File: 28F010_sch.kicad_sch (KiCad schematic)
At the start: 13 parts, among them U10 74LVC1G332, U11 74LS138, U12 CY7C199, U15 CY7C199, U16 4012, U17 CY7C199, U3 74LS04, U39 74LS04, U40 4012, U8 74LS138, U9 CY7C199

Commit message: pcb wiring
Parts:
- U16: footprint Package_DIP:DIP-12_W7.62mm -> (none)
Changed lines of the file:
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@@
     (property "Reference" "U16" (id 0) (at 111.76 8.89 0))
     (property "Value" "4012" (id 1) (at 111.76 11.43 0))
-    (property "Footprint" "Package_DIP:DIP-12_W7.62mm" (id 2) (at 111.76 19.05 0)
+    (property "Footprint" "" (id 2) (at 111.76 19.05 0)
       (effects (font (size 1.27 1.27)) hide)
     )
@@
     (property "Reference" "U16" (id 0) (at 111.76 19.05 0))
     (property "Value" "4012" (id 1) (at 111.76 21.59 0))
-    (property "Footprint" "Package_DIP:DIP-12_W7.62mm" (id 2) (at 111.76 29.21 0)
-      (effects (font (size 1.27 1.27)) hide)
-    )
+    (property "Footprint" "" (id 2) (at 111.76 29.21 0)
+      (effects (font (size 1.27 1.27)) hide)
+    )

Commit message: More PCB wiring
Wired all components to eachother, did not interface everything with the 8086
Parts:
- U16: footprint (none) -> Package_DIP:DIP-14_W7.62mm
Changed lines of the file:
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@@
     (property "Reference" "U16" (id 0) (at 111.76 8.89 0))
     (property "Value" "4012" (id 1) (at 111.76 11.43 0))
-    (property "Footprint" "" (id 2) (at 111.76 19.05 0)
+    (property "Footprint" "Package_DIP:DIP-14_W7.62mm" (id 2) (at 111.76 19.05 0)
       (effects (font (size 1.27 1.27)) hide)
     )
@@
     (property "Reference" "U16" (id 0) (at 111.76 19.05 0))
     (property "Value" "4012" (id 1) (at 111.76 21.59 0))
-    (property "Footprint" "" (id 2) (at 111.76 29.21 0)
-      (effects (font (size 1.27 1.27)) hide)
-    )
+    (property "Footprint" "Package_DIP:DIP-14_W7.62mm" (id 2) (at 111.76 29.21 0)
+      (effects (font (size 1.27 1.27)) hide)
+    )

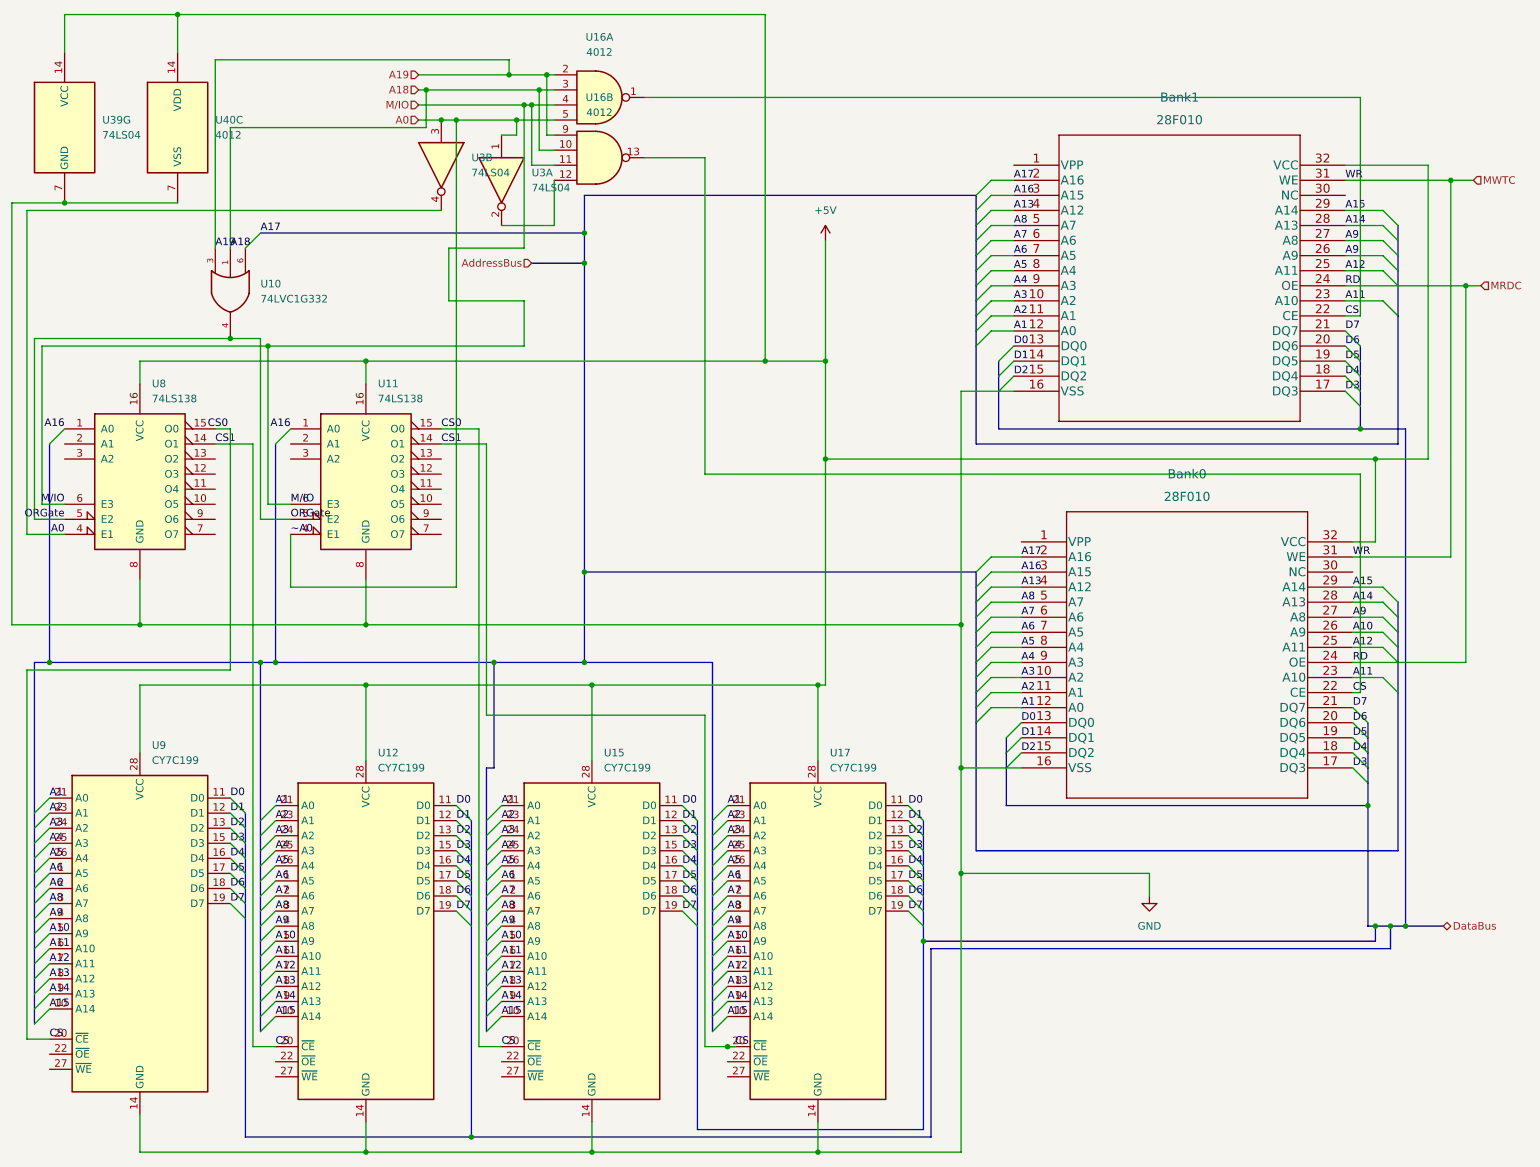
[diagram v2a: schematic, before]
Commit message: Fixed Incorrect Data Pin labels in memory
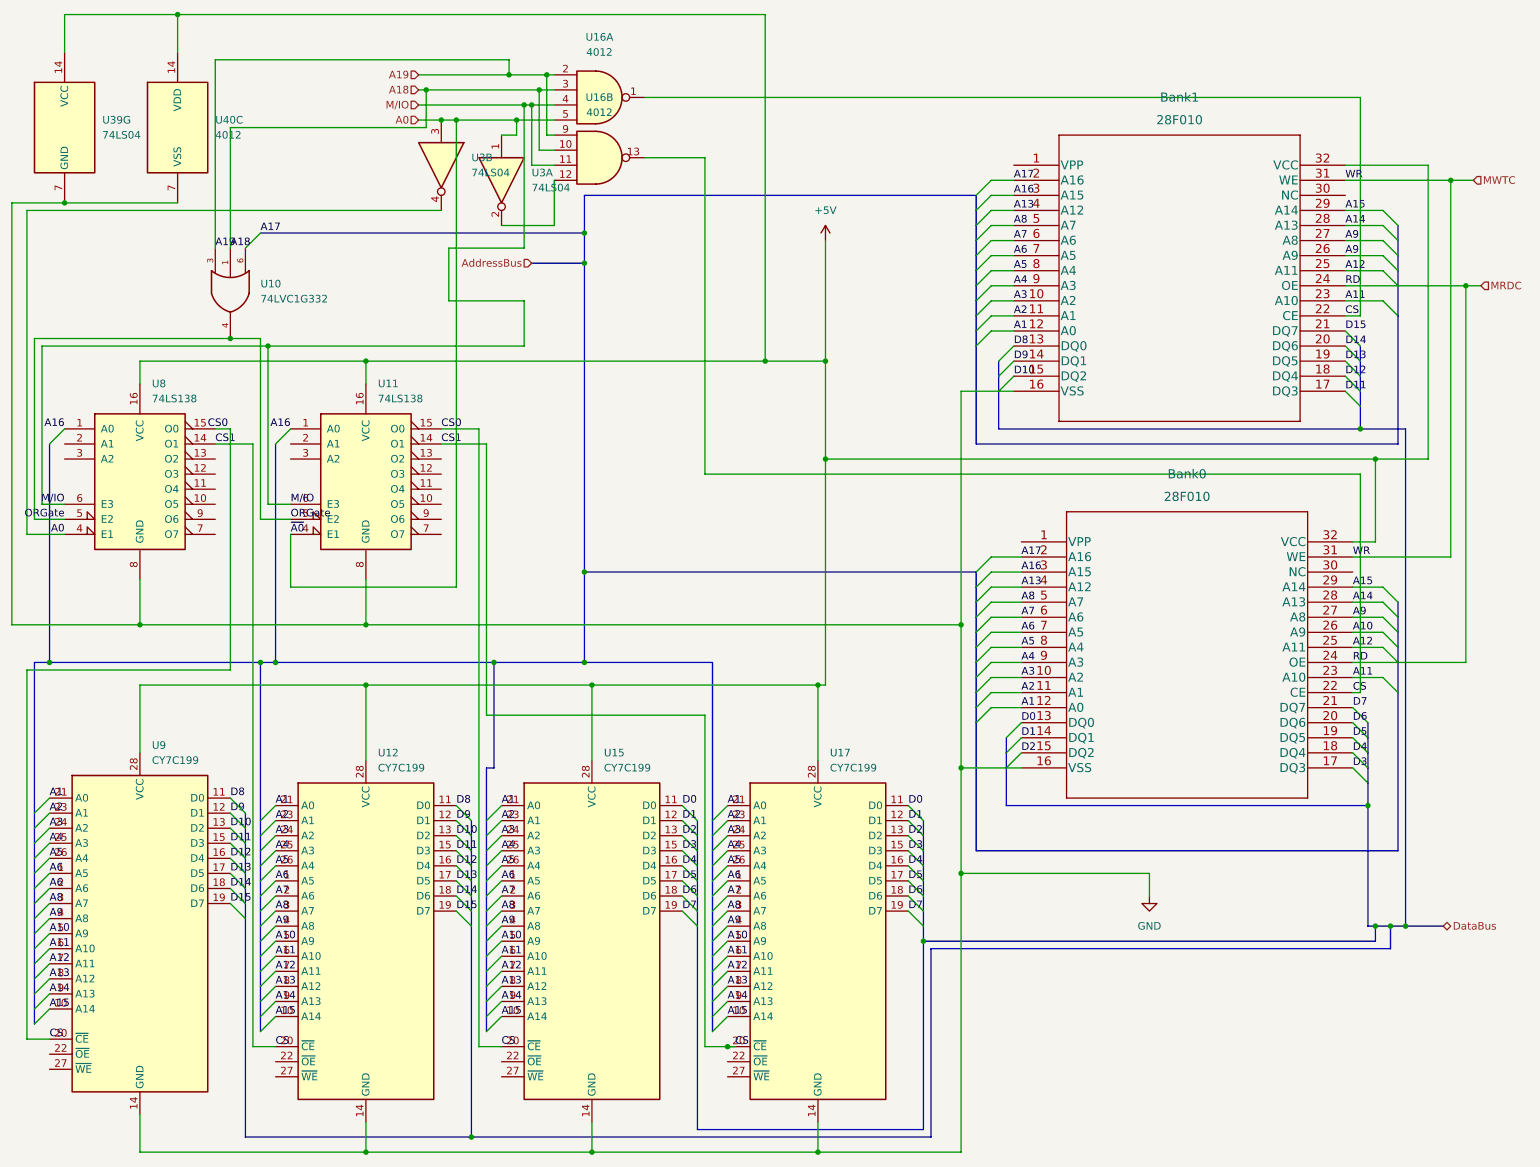
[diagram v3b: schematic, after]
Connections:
- net D0: no longer Bank1.13 (DQ0), U12.11 (D0), U9.11 (D0)
- net D1: no longer Bank1.14 (DQ1), U12.12 (D1), U9.12 (D1)
- net D2: no longer Bank1.15 (DQ2), U12.13 (D2), U9.13 (D2)
- net D3: no longer Bank1.17 (DQ3), U12.15 (D3), U9.15 (D3)
- net D4: no longer Bank1.18 (DQ4), U12.16 (D4), U9.16 (D4)
- net D5: no longer Bank1.19 (DQ5), U12.17 (D5), U9.17 (D5)
- net D6: no longer Bank1.20 (DQ6), U12.18 (D6), U9.18 (D6)
- net D7: no longer Bank1.21 (DQ7), U12.19 (D7), U9.19 (D7)
- new net D10: Bank1.15 (DQ2), U12.13 (D2), U9.13 (D2)
- new net D11: Bank1.17 (DQ3), U12.15 (D3), U9.15 (D3)
- new net D12: Bank1.18 (DQ4), U12.16 (D4), U9.16 (D4)
- new net D13: Bank1.19 (DQ5), U12.17 (D5), U9.17 (D5)
- new net D14: Bank1.20 (DQ6), U12.18 (D6), U9.18 (D6)
- new net D15: Bank1.21 (DQ7), U12.19 (D7), U9.19 (D7)
- new net D8: Bank1.13 (DQ0), U12.11 (D0), U9.11 (D0)
- new net D9: Bank1.14 (DQ1), U12.12 (D1), U9.12 (D1)
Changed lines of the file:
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@@
     (effects (font (size 1.27 1.27)) (justify left bottom))
   )
-  (label "D3" (at 49.53 144.78 0)
+  (label "D15" (at 49.53 154.94 0)
     (effects (font (size 1.27 1.27)) (justify left bottom))
   )
@@
   )
   (label "A8" (at 181.61 40.64 0)
-    (effects (font (size 1.27 1.27)) (justify left bottom))
-  )
-  (label "D1" (at 49.53 139.7 0)
     (effects (font (size 1.27 1.27)) (justify left bottom))
   )
@@
     (effects (font (size 1.27 1.27)) (justify left bottom))
   )
-  (label "~A0" (at 59.69 92.71 0)
+  (label "~{A0}" (at 59.69 92.71 0)
+    (effects (font (size 1.27 1.27)) (justify left bottom))
+  )
+  (label "D11" (at 87.63 146.05 0)
     (effects (font (size 1.27 1.27)) (justify left bottom))
   )
@@
     (effects (font (size 1.27 1.27)) (justify left bottom))
   )
-  (label "D6" (at 87.63 153.67 0)
-    (effects (font (size 1.27 1.27)) (justify left bottom))
-  )
   (label "A11" (at 133.35 163.83 0)
     (effects (font (size 1.27 1.27)) (justify left bottom))
@@
     (effects (font (size 1.27 1.27)) (justify left bottom))
   )
+  (label "D13" (at 49.53 149.86 0)
+    (effects (font (size 1.27 1.27)) (justify left bottom))
+  )
   (label "A1" (at 133.35 138.43 0)
     (effects (font (size 1.27 1.27)) (justify left bottom))
@@
     (effects (font (size 1.27 1.27)) (justify left bottom))
   )
-  (label "D3" (at 87.63 146.05 0)
+  (label "D15" (at 87.63 156.21 0)
+    (effects (font (size 1.27 1.27)) (justify left bottom))
+  )
+  (label "D11" (at 49.53 144.78 0)
     (effects (font (size 1.27 1.27)) (justify left bottom))
   )
@@
   )
   (label "D7" (at 238.76 121.92 0)
+    (effects (font (size 1.27 1.27)) (justify left bottom))
+  )
+  (label "D9" (at 49.53 139.7 0)
     (effects (font (size 1.27 1.27)) (justify left bottom))
   )
@@
     (effects (font (size 1.27 1.27)) (justify left bottom))
   )
-  (label "D5" (at 49.53 149.86 0)
-    (effects (font (size 1.27 1.27)) (justify left bottom))
-  )
   (label "A13" (at 181.61 38.1 0)
     (effects (font (size 1.27 1.27)) (justify left bottom))
   )
-  (label "D7" (at 237.49 58.42 0)
+  (label "D15" (at 237.49 58.42 0)
     (effects (font (size 1.27 1.27)) (justify left bottom))
   )
@@
     (effects (font (size 1.27 1.27)) (justify left bottom))
   )
-  (label "D4" (at 49.53 147.32 0)
-    (effects (font (size 1.27 1.27)) (justify left bottom))
-  )
   (label "A2" (at 95.25 140.97 0)
     (effects (font (size 1.27 1.27)) (justify left bottom))
@@
     (effects (font (size 1.27 1.27)) (justify left bottom))
   )
-  (label "D3" (at 237.49 68.58 0)
+  (label "D11" (at 237.49 68.58 0)
     (effects (font (size 1.27 1.27)) (justify left bottom))
   )
@@
     (effects (font (size 1.27 1.27)) (justify left bottom))
   )
-  (label "D0" (at 181.61 60.96 0)
+  (label "D8" (at 181.61 60.96 0)
     (effects (font (size 1.27 1.27)) (justify left bottom))
   )
@@
     (effects (font (size 1.27 1.27)) (justify right bottom))
   )
-  (label "D2" (at 181.61 66.04 0)
+  (label "D13" (at 87.63 151.13 0)
+    (effects (font (size 1.27 1.27)) (justify left bottom))
+  )
+  (label "D10" (at 181.61 66.04 0)
     (effects (font (size 1.27 1.27)) (justify left bottom))
   )
@@
     (effects (font (size 1.27 1.27)) (justify left bottom))
   )
-  (label "D6" (at 237.49 60.96 0)
+  (label "D14" (at 237.49 60.96 0)
     (effects (font (size 1.27 1.27)) (justify left bottom))
   )
@@
   )
   (label "A9" (at 238.76 106.68 0)
+    (effects (font (size 1.27 1.27)) (justify left bottom))
+  )
+  (label "D8" (at 49.53 137.16 0)
     (effects (font (size 1.27 1.27)) (justify left bottom))
   )
@@
     (effects (font (size 1.27 1.27)) (justify left bottom))
   )
-  (label "D7" (at 87.63 156.21 0)
-    (effects (font (size 1.27 1.27)) (justify left bottom))
-  )
   (label "A11" (at 19.05 162.56 0)
     (effects (font (size 1.27 1.27)) (justify left bottom))
   )
-  (label "D4" (at 87.63 148.59 0)
-    (effects (font (size 1.27 1.27)) (justify left bottom))
-  )
   (label "A7" (at 182.88 106.68 0)
     (effects (font (size 1.27 1.27)) (justify left bottom))
@@
     (effects (font (size 1.27 1.27)) (justify left bottom))
   )
+  (label "D12" (at 87.63 148.59 0)
+    (effects (font (size 1.27 1.27)) (justify left bottom))
+  )
+  (label "D9" (at 87.63 140.97 0)
+    (effects (font (size 1.27 1.27)) (justify left bottom))
+  )
   (label "D5" (at 238.76 127 0)
     (effects (font (size 1.27 1.27)) (justify left bottom))
   )
+  (label "D10" (at 49.53 142.24 0)
+    (effects (font (size 1.27 1.27)) (justify left bottom))
+  )
   (label "A14" (at 237.49 40.64 0)
     (effects (font (size 1.27 1.27)) (justify left bottom))
@@
     (effects (font (size 1.27 1.27)) (justify left bottom))
   )
-  (label "D7" (at 49.53 154.94 0)
+  (label "D10" (at 87.63 143.51 0)
     (effects (font (size 1.27 1.27)) (justify left bottom))
   )
@@
     (effects (font (size 1.27 1.27)) (justify left bottom))
   )
-  (label "D6" (at 49.53 152.4 0)
+  (label "D8" (at 87.63 138.43 0)
     (effects (font (size 1.27 1.27)) (justify left bottom))
   )
@@
     (effects (font (size 1.27 1.27)) (justify left bottom))
   )
+  (label "D14" (at 49.53 152.4 0)
+    (effects (font (size 1.27 1.27)) (justify left bottom))
+  )
   (label "D3" (at 125.73 146.05 0)
     (effects (font (size 1.27 1.27)) (justify left bottom))
@@
     (effects (font (size 1.27 1.27)) (justify left bottom))
   )
+  (label "D12" (at 49.53 147.32 0)
+    (effects (font (size 1.27 1.27)) (justify left bottom))
+  )
   (label "A5" (at 95.25 148.59 0)
     (effects (font (size 1.27 1.27)) (justify left bottom))
@@
     (effects (font (size 1.27 1.27)) (justify left bottom))
   )
-  (label "D1" (at 87.63 140.97 0)
-    (effects (font (size 1.27 1.27)) (justify left bottom))
-  )
-  (label "D0" (at 49.53 137.16 0)
-    (effects (font (size 1.27 1.27)) (justify left bottom))
-  )
   (label "D4" (at 125.73 148.59 0)
     (effects (font (size 1.27 1.27)) (justify left bottom))
   )
-  (label "D4" (at 237.49 66.04 0)
+  (label "D12" (at 237.49 66.04 0)
     (effects (font (size 1.27 1.27)) (justify left bottom))
   )
@@
     (effects (font (size 1.27 1.27)) (justify left bottom))
   )
-  (label "D0" (at 87.63 138.43 0)
-    (effects (font (size 1.27 1.27)) (justify left bottom))
-  )
   (label "A2" (at 133.35 140.97 0)
     (effects (font (size 1.27 1.27)) (justify left bottom))
@@
     (effects (font (size 1.27 1.27)) (justify left bottom))
   )
-  (label "D5" (at 237.49 63.5 0)
+  (label "D13" (at 237.49 63.5 0)
+    (effects (font (size 1.27 1.27)) (justify left bottom))
+  )
+  (label "D14" (at 87.63 153.67 0)
     (effects (font (size 1.27 1.27)) (justify left bottom))
   )
@@
     (effects (font (size 1.27 1.27)) (justify left bottom))
   )
-  (label "D2" (at 87.63 143.51 0)
-    (effects (font (size 1.27 1.27)) (justify left bottom))
-  )
   (label "A9" (at 95.25 158.75 0)
     (effects (font (size 1.27 1.27)) (justify left bottom))
   )
-  (label "D5" (at 87.63 151.13 0)
-    (effects (font (size 1.27 1.27)) (justify left bottom))
-  )
   (label "A7" (at 95.25 153.67 0)
     (effects (font (size 1.27 1.27)) (justify left bottom))
@@
     (effects (font (size 1.27 1.27)) (justify left bottom))
   )
-  (label "D2" (at 49.53 142.24 0)
-    (effects (font (size 1.27 1.27)) (justify left bottom))
-  )
   (label "D1" (at 182.88 127 0)
     (effects (font (size 1.27 1.27)) (justify left bottom))
   )
-  (label "D1" (at 181.61 63.5 0)
-    (effects (font (size 1.27 1.27)) (justify left bottom))
-  )
+  (label "D9" (at 181.61 63.5 0)
+    (effects (font (size 1.27 1.27)) (justify left bottom))
+  )
